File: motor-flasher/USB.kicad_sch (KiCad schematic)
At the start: 26 parts, among them J1 USB4105-GF-A, J12 TS-102-G-A, J4 B2B-PH-K-S-GW, U6 TPS61027DRCR, U7 BQ24075RGTT

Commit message: Starting layout
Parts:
- removed C10, C9: 4.7uF, Capacitor_SMD:C_0402_1005Metric, symbol Device:C
- removed C8: 1uF, Capacitor_SMD:C_0402_1005Metric, symbol Device:C
- removed J12: TS-102-G-A, TS_102_G_A:SAMTEC_TS-102-G-A, symbol TS-102-G-A:TS-102-G-A
- removed R11, R12, R9: 10k, Resistor_SMD:R_0402_1005Metric, symbol Device:R
- removed R14: 1.18K, Resistor_SMD:R_0402_1005Metric, symbol Device:R
- removed R15: 25k, Resistor_SMD:R_0805_2012Metric, symbol Device:R
- removed R17: 1.5k, Resistor_SMD:R_0402_1005Metric, symbol Device:R
- removed U7: BQ24075RGTT, revparts2:QFN50P300X300X100-17N, symbol BQ24075RGTT:BQ24075RGTT
- added SW2: SS12D07VG4NSGAPA, revparts2:SS12D07_CNK, symbol 2024-05-28_19-32-11:SS12D07VG4NSGAPA
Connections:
- net VCC: now also SW2.3; no longer C3.1, C4.1, L2.1, R3.1, U6.1 (EN), U6.6 (VBAT)
- net VDD: now also CR2.1, SW2.1
- new net Vout: C3.1, C4.1, L2.1, R3.1, SW2.2, U6.1 (EN), U6.6 (VBAT)

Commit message: Beginning Layout Process
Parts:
- CR2: footprint smd110:SOD-123FL_MCC -> Motor-Flasher:SOD-123FL_MCC
- J1: value USB4105-GF-A -> TYPE-C 16PIN 2MD(073); footprint revparts2:GCT_USB4105-GF-A -> Motor-Flasher:GCT_USB4105-GF-A
- J4: footprint revparts2:JST_B2B-XH-A -> Motor-Flasher:JST_B2B-XH-A
- L2: footprint revparts3:CDRH5D28RHP -> Motor-Flasher:CDRH5D28RHP
- SW2: footprint revparts2:SS12D07_CNK -> Motor-Flasher:SS12D07_CNK
- U6: footprint revparts2:VREG_V62_16624-01YE -> Motor-Flasher:VREG_V62_16624-01YE
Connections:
- net GND: now also C3.1, C4.1; no longer C3.2, C4.2
- net Vout: now also C3.2, C4.2; no longer C3.1, C4.1
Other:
- note removed: "Determine how long you want to charge by the calculation C(nF)/34.3 = X hours This is the capacitor attached to CT"
- note removed: "Inductor Current rated for at least 1.2 A 3.3uH Resistance values of 3.45MOhms by 250k"
- moved on the sheet: C3, C4, C5, C6, CR2, J1, J4, L2, R1, R2, R3, R4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

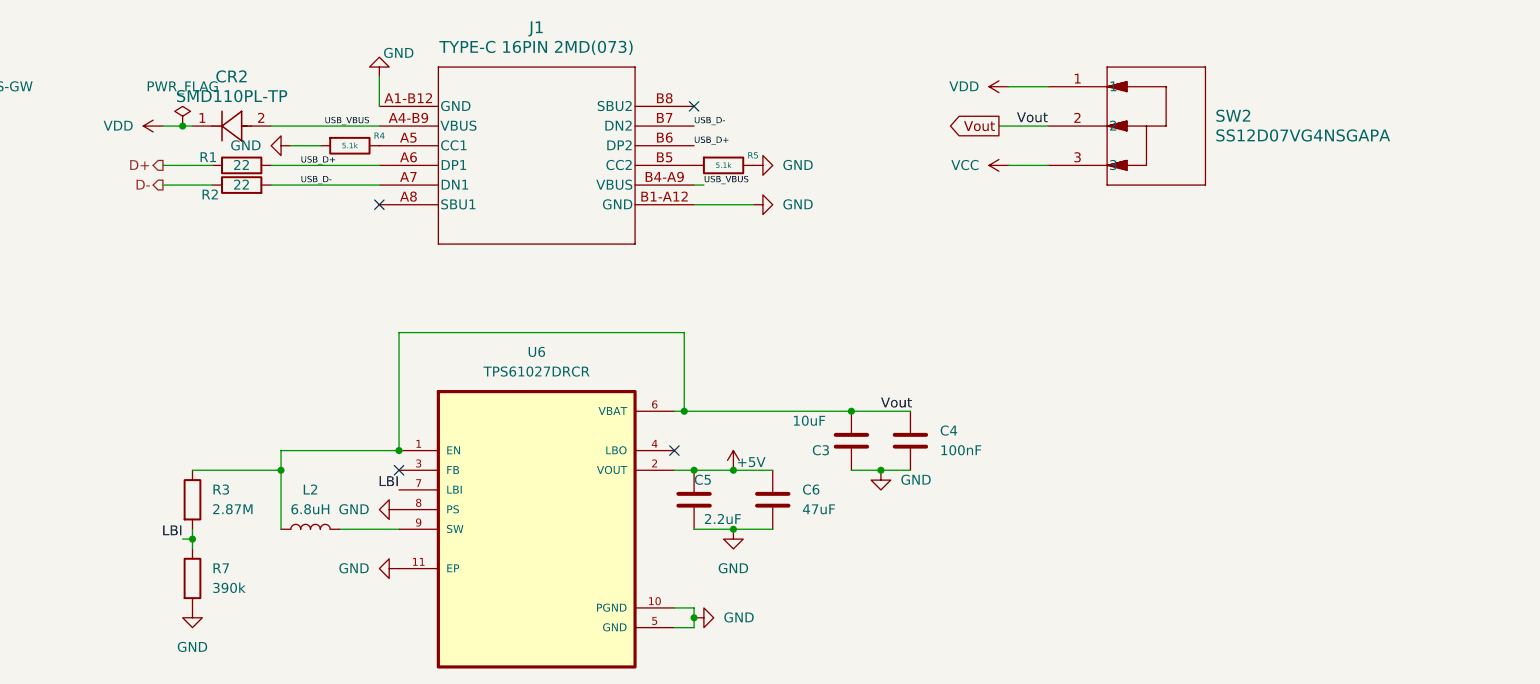
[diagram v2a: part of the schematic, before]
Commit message: Removed ERC Errors and Warnings
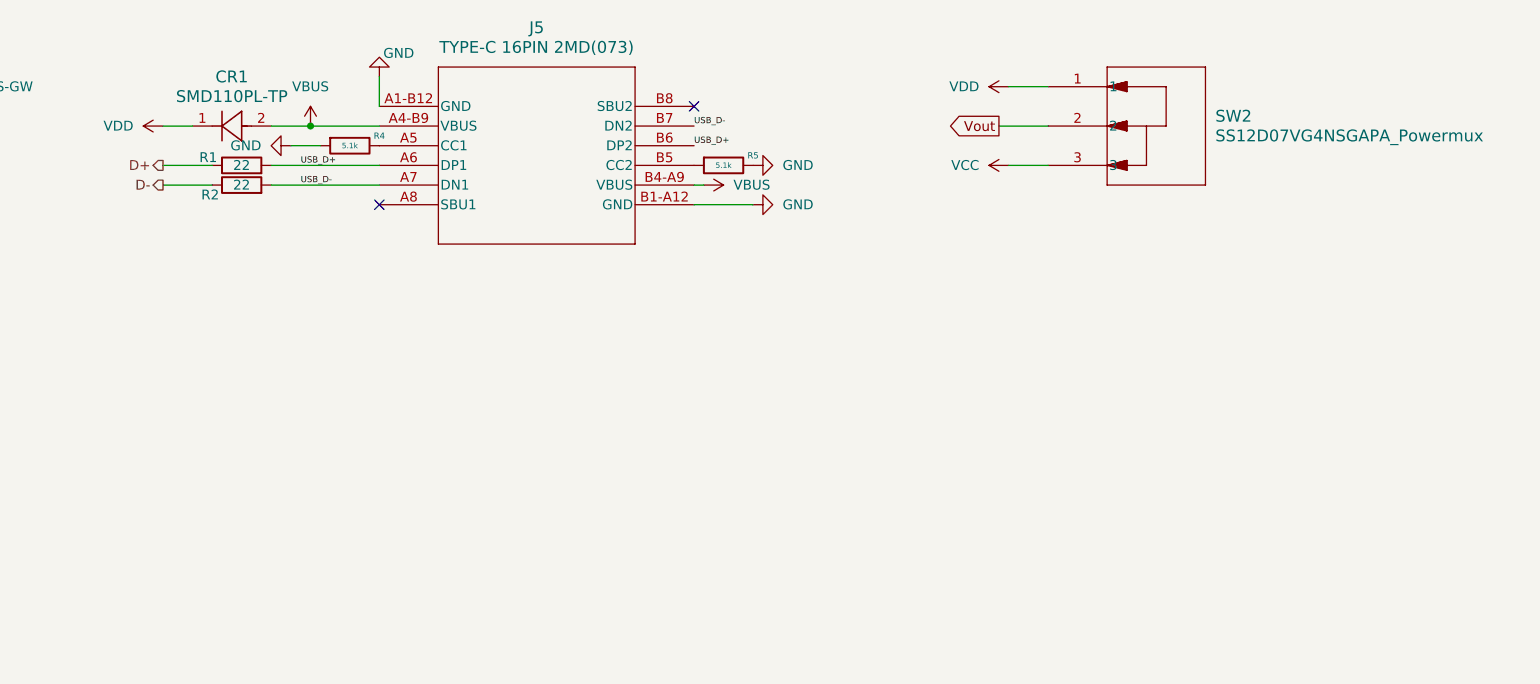
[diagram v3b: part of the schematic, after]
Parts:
- removed C3: 10uF, Capacitor_SMD:C_0805_2012Metric, symbol Device:C
- removed C4: 100nF, Capacitor_SMD:C_0402_1005Metric, symbol Device:C
- removed C5: 2.2uF, Capacitor_SMD:C_0402_1005Metric, symbol Device:C
- removed C6: 47uF, Capacitor_SMD:C_0805_2012Metric, symbol Device:C
- removed CR2: SMD110PL-TP, Motor-Flasher:SOD-123FL_MCC, symbol 2024-05-16_18-19-58:SMD110PL-TP
- removed J1: TYPE-C 16PIN 2MD(073), Motor-Flasher:GCT_USB4105-GF-A, symbol 2024-05-13_21-06-25:USB4105-GF-A
- removed L2: 6.8uH, Motor-Flasher:CDRH5D28RHP, symbol Device:L
- removed R3: 2.87M, Resistor_SMD:R_0805_2012Metric, symbol Device:R
- removed R7: 390k, Resistor_SMD:R_0805_2012Metric, symbol Device:R
- removed SW2: SS12D07VG4NSGAPA, Motor-Flasher:SS12D07_CNK, symbol 2024-05-28_19-32-11:SS12D07VG4NSGAPA
- removed U6: TPS61027DRCR, Motor-Flasher:VREG_V62_16624-01YE, symbol TPS61027DRCR:TPS61027DRCR
- added CR1: SMD110PL-TP, Motor-Flasher:SOD-123FL_MCC, symbol Motor_Flasher_Modified:SMD110PL-TP
- added J5: TYPE-C 16PIN 2MD(073), Motor-Flasher:GCT_USB4105-GF-A, symbol Motor_Flasher_Modified:TYPE-C_16PIN_2MD(073)
- added SW2: SS12D07VG4NSGAPA_Powermux, Motor-Flasher:SS12D07_CNK, symbol Motor_Flasher_Modified:SS12D07VG4NSGAPA_Powermux
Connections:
- net GND: now also J5.A1-B12 (GND), J5.B1-A12 (GND)
- net USB_D+: now also J5.A6 (DP1), J5.B6 (DP2)
- net USB_D-: now also J5.A7 (DN1), J5.B7 (DN2)
- net VCC: now also SW2.3
- net VDD: now also CR1.1, SW2.1
- net Vout: now also SW2.2
- net at R4.1: now also J5.A5 (CC1)
- net at R5.2: now also J5.B5 (CC2)
- new net VBUS: CR1.2, J5.A4-B9 (VBUS), J5.B4-A9 (VBUS)
- no-connect marks 4 -> 2

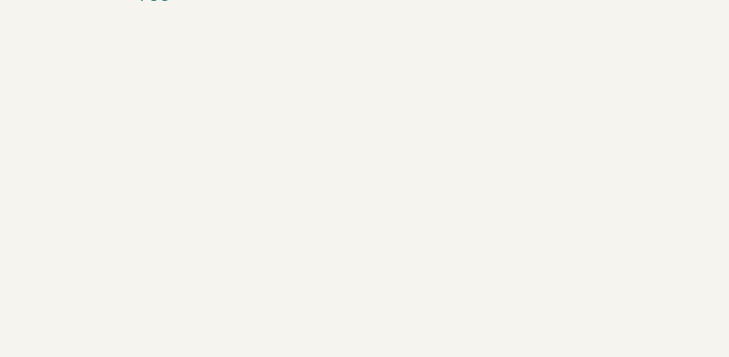
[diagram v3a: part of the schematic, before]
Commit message: Rough Placement and Design
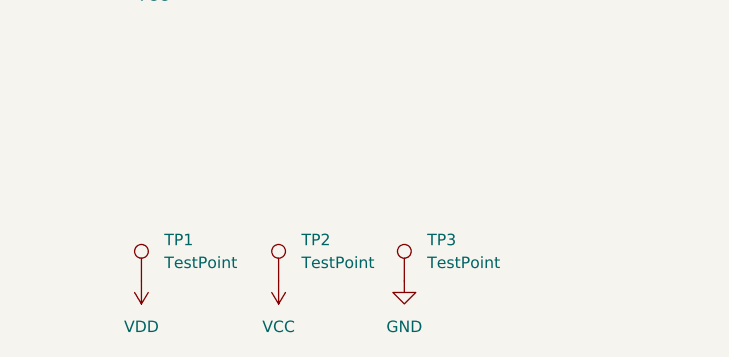
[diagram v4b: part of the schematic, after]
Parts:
- added TP1, TP2, TP3: TestPoint, symbol Connector:TestPoint
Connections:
- net GND: now also TP3.1
- net VCC: now also TP2.1
- net VDD: now also TP1.1

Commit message: Saving current revision
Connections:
- net VDD: now also J5.A4-B9 (VBUS), J5.B4-A9 (VBUS); no longer CR1.1
- net Vout: now also CR1.1; no longer SW2.2
- removed net VBUS: CR1.2, J5.A4-B9 (VBUS), J5.B4-A9 (VBUS)
- new net: CR1.2, SW2.2
